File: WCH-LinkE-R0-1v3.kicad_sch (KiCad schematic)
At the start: 38 parts, among them Q1 DMG1012UW-7, Q2 DMG1012UW-7, SW1 SKRPASE010, SW2 SKRPASE010, SW3 SKRPASE010

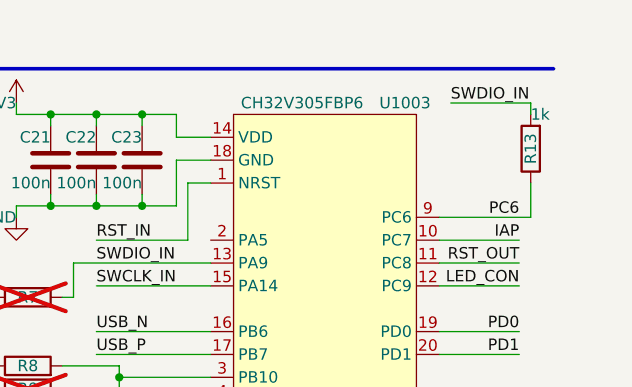
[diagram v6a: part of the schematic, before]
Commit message: Change J3 and J4 part numbers
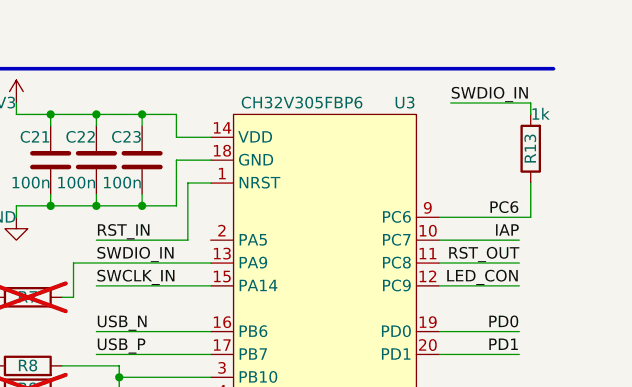
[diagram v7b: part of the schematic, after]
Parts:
- renumbered U1003 to U3
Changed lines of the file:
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@@
   (symbol (lib_id "Tiny_Scarab:CH32V305FBP6") (at 171.45 39.37 0) (unit 1)
     (in_bom yes) (on_board yes) (dnp no)
-    (property "Reference" "U1003" (at 180.34 22.86 0)
+    (property "Reference" "U3" (at 180.34 22.86 0)
       (effects (font (size 1.27 1.27)))
     )
@@
       (project "tiny-scarab"
         (path "/156c5422-ee07-49a4-8263-a2dbd26b90bd/90393844-9805-4207-88e8-abd4029c5b43"
-          (reference "U1003") (unit 1)
+          (reference "U3") (unit 1)
         )
       )

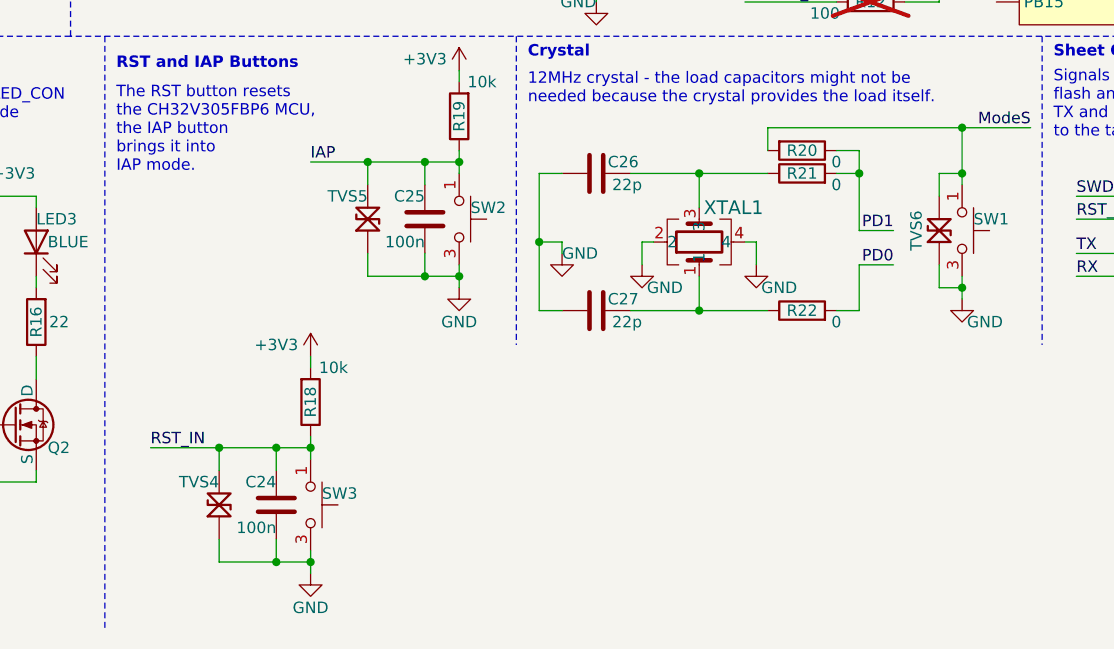
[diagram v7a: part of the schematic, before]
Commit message: Replace TVS diodes with cheaper alternative
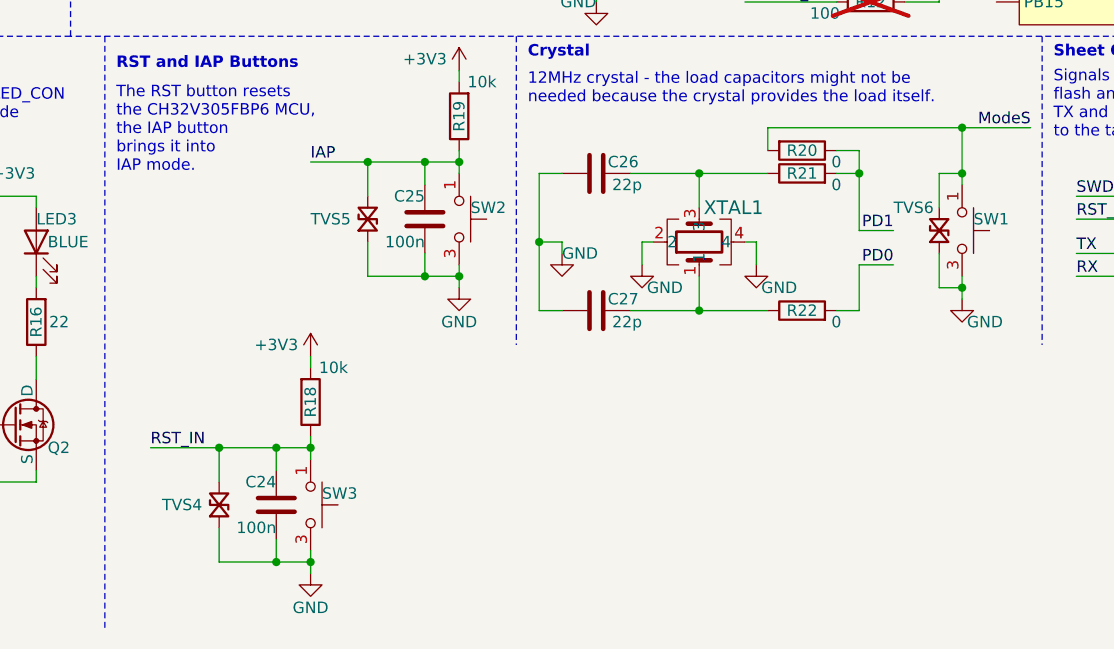
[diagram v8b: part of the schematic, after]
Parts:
- removed TVS4, TVS5, TVS6: 5V, Tiny_Scarab:D_SOD-323_CDSOD323-T05LC, symbol Tiny_Scarab:CDSOD323-T05LC
- added TVS4, TVS5, TVS6: 5V, Tiny_Scarab:D_SOD-882_SP1007-01ETG, symbol Tiny_Scarab:TVS_SP1007-01ETG
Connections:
- net GND: now also TVS4.2, TVS5.2, TVS6.2
- net IAP: now also TVS5.1
- net ModeS: now also TVS6.1
- net RST_IN: now also TVS4.1
